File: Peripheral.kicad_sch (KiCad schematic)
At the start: 25 parts, among them J2 Conn_02x05_Odd_Even, J3 Conn_02x08_Odd_Even, J4 Conn_02x08_Odd_Even, J6 Bus_ISA_8bit, J7 Conn_02x17_Odd_Even, J8 TTL UART, U25 SN74LS07N, U3 74164, U31 TXS0104ED, U32 16550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

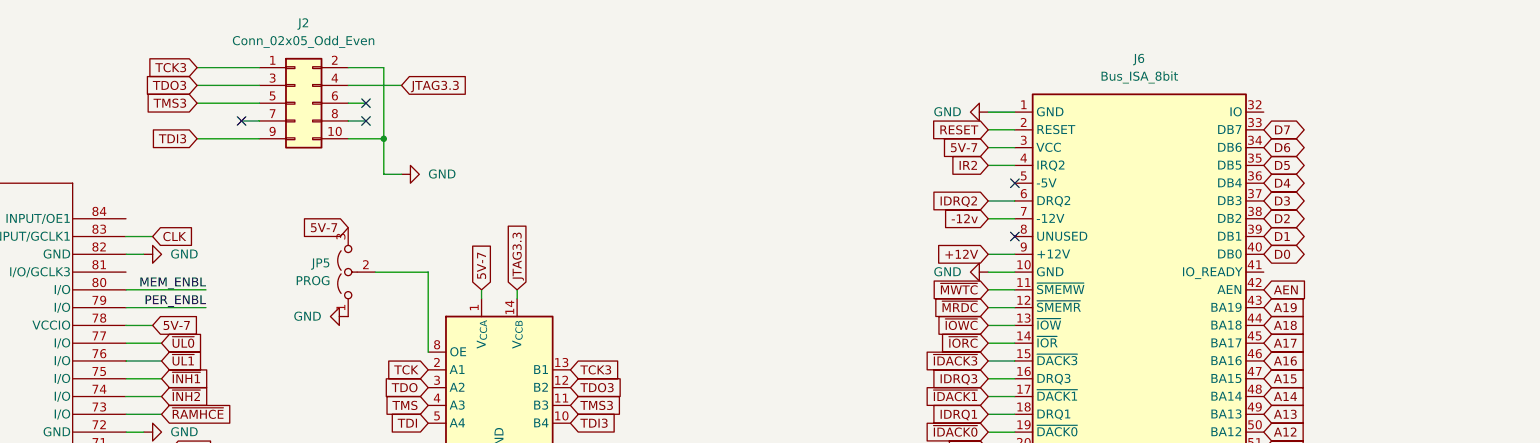
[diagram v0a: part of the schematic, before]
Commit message: Adjusted Data Bus for 80130
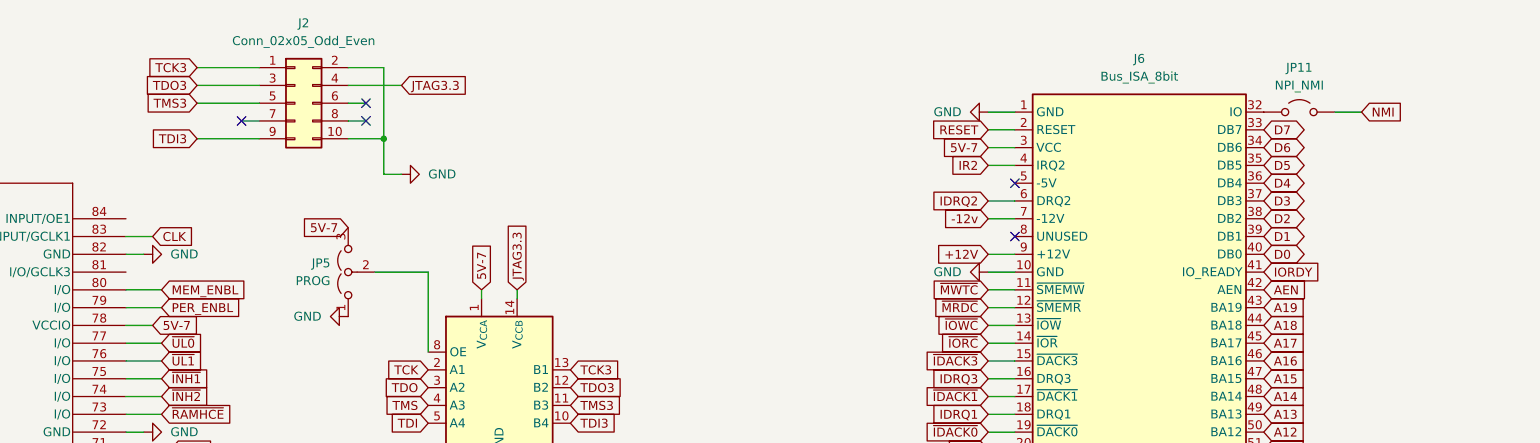
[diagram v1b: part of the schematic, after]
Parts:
- added JP11: NPI_NMI, symbol Jumper:Jumper_2_Open
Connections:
- net at J6.32 (IO): now also JP11.1 (A)
- net IORDY: now reaches J6.41 (IO_READY)
- new net NMI: JP11.2 (B)
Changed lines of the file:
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@@
 	(wire
 		(pts
-			(xy 163.83 55.88) (xy 152.4 55.88)
+			(xy 157.48 55.88) (xy 152.4 55.88)
 		)
 		(stroke
@@
 	(wire
 		(pts
-			(xy 163.83 58.42) (xy 152.4 58.42)
+			(xy 157.48 58.42) (xy 152.4 58.42)
 		)
 		(stroke
@@
 	(wire
 		(pts
+			(xy 328.93 30.48) (xy 325.12 30.48)
+		)
+		(stroke
+			(width 0)
+			(type default)
+		)
+	)
+	(wire
+		(pts
 			(xy 158.75 127) (xy 152.4 127)
 		)
@@
 	)
 	(label "MEM_ENBL"
-		(at 163.83 55.88 180)
-		(effects
-			(font
-				(size 1.27 1.27)
-			)
-			(justify right bottom)
-		)
-	)
-	(label "PER_ENBL"
-		(at 163.83 58.42 180)
-		(effects
-			(font
-				(size 1.27 1.27)
-			)
-			(justify right bottom)
-		)
-	)
-	(label "MEM_ENBL"
 		(at 40.64 261.62 0)
 		(effects
@@
 		)
 	)
+	(global_label "PER_ENBL"
+		(shape input)
+		(at 157.48 58.42 0)
+		(fields_autoplaced yes)
+		(effects
+			(font
+				(size 1.27 1.27)
+			)
+			(justify left)
+		)
+		(property "Intersheetrefs" "${INTERSHEET_REFS}"
+			(at 169.8994 58.42 0)
+			(effects
+				(font
+					(size 1.27 1.27)
+				)
+				(justify left)
+				(hide yes)
+			)
+		)
+	)
 	(global_label "~{MRDC}"
 		(shape input)
@@
 		)
 	)
+	(global_label "NMI"
+		(shape input)
+		(at 328.93 30.48 0)
+		(fields_autoplaced yes)
+		(effects
+			(font
+				(size 1.27 1.27)
+			)
+			(justify left)
+		)
+		(property "Intersheetrefs" "${INTERSHEET_REFS}"
+			(at 335.3019 30.48 0)
+			(effects
+				(font
+					(size 1.27 1.27)
+				)
+				(justify left)
+				(hide yes)
+			)
+		)
+	)
 	(global_label "~{IDACK0}"
 		(shape input)
@@
 		)
 	)
+	(global_label "IORDY"
+		(shape input)
+		(at 314.96 53.34 0)
+		(fields_autoplaced yes)
+		(effects
+			(font
+				(size 1.27 1.27)
+			)
+			(justify left)
+		)
+		(property "Intersheetrefs" "${INTERSHEET_REFS}"
+			(at 323.5091 53.34 0)
+			(effects
+				(font
+					(size 1.27 1.27)
+				)
+				(justify left)
+				(hide yes)
+			)
+		)
+	)
 	(global_label "A13"
 		(shape input)
@@
 		)
 	)
+	(global_label "MEM_ENBL"
+		(shape input)
+		(at 157.48 55.88 0)
+		(fields_autoplaced yes)
+		(effects
+			(font
+				(size 1.27 1.27)
+			)
+			(justify left)
+		)
+		(property "Intersheetrefs" "${INTERSHEET_REFS}"
+			(at 170.2622 55.88 0)
+			(effects
+				(font
+					(size 1.27 1.27)
+				)
+				(justify left)
+				(hide yes)
+			)
+		)
+	)
 	(global_label "5V-7"
 		(shape input)
@@
 					(unit 1)
 				)
+			)
+		)
+	)
+	(symbol
+		(lib_id "Jumper:Jumper_2_Open")
+		(at 320.04 30.48 0)
+		(unit 1)
+		(exclude_from_sim no)
+		(in_bom yes)
+		(on_board yes)
+		(dnp no)
+		(fields_autoplaced yes)
+		(property "Reference" "JP11"
+			(at 320.04 24.13 0)
+			(effects
+				(font
+					(size 1.27 1.27)
+				)
+			)
+		)
+		(property "Value" "NPI_NMI"
+			(at 320.04 26.67 0)
+			(effects
+				(font
+					(size 1.27 1.27)
+				)
+			)
+		)
+		(property "Footprint" ""
+			(at 320.04 30.48 0)
+			(effects
+				(font
+					(size 1.27 1.27)
+				)
+				(hide yes)
+			)
+		)
+		(property "Datasheet" "~"
+			(at 320.04 30.48 0)
+			(effects
+				(font
+					(size 1.27 1.27)
+				)
+				(hide yes)
+			)
+		)
+		(property "Description" "Jumper, 2-pole, open"
+			(at 320.04 30.48 0)
+			(effects
+				(font
+					(size 1.27 1.27)
+				)
+				(hide yes)
+			)
+		)
+		(pin "1"
+		)
+		(pin "2"
+		)
+		(instances
+			(project "8086MAX_SBC"
+				(path "/f3556896-fb91-4e69-9fe8-87bb2814f9d4/130d313c-ef1b-459f-b12a-6a2f6b18a216"
+					(reference "JP11")
+					(unit 1)
+				)

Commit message: assigned all footprints
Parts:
- C10, C11, C12, C13: footprint (none) -> Capacitor_THT:C_Disc_D8.0mm_W2.5mm_P5.00mm
- J2: footprint (none) -> Connector_PinHeader_2.54mm:PinHeader_2x05_P2.54mm_Vertical
- J3, J4: footprint (none) -> Connector_PinHeader_2.54mm:PinHeader_2x08_P2.54mm_Vertical
- J6: footprint (none) -> 7-5530843-0:TE_7-5530843-0
- J7: footprint (none) -> Connector_IDC:IDC-Header_2x17_P2.54mm_Latch_Vertical
- J8: footprint (none) -> Connector_PinHeader_2.54mm:PinHeader_1x05_P2.54mm_Vertical
- JP10, JP11, JP7, JP8, JP9: footprint (none) -> Connector_PinHeader_2.54mm:PinHeader_1x02_P2.54mm_Vertical
- JP5: footprint (none) -> Connector_PinHeader_2.54mm:PinHeader_1x03_P2.54mm_Vertical
- U25, U3, U6: footprint (none) -> Package_DIP:DIP-14_W7.62mm
- U33: footprint (none) -> Package_LCC:PLCC-44_THT-Socket
- U9: footprint PLCC84_MCH -> Package_LCC:PLCC-84_29.3x29.3mm_P1.27mm
- Y2, Y3: footprint (none) -> Crystal:Crystal_HC49-U_Vertical
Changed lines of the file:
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@@
 			)
 		)
-		(property "Footprint" ""
+		(property "Footprint" "Connector_PinHeader_2.54mm:PinHeader_2x05_P2.54mm_Vertical"
 			(at 176.53 29.21 0)
 			(effects
@@
 			)
 		)
-		(property "Footprint" ""
+		(property "Footprint" "Capacitor_THT:C_Disc_D8.0mm_W2.5mm_P5.00mm"
 			(at 300.6852 365.76 0)
 			(effects
@@
 			)
 		)
-		(property "Footprint" ""
+		(property "Footprint" "Connector_PinHeader_2.54mm:PinHeader_1x02_P2.54mm_Vertical"
 			(at 320.04 30.48 0)
 			(effects
@@
 			)
 		)
-		(property "Footprint" ""
+		(property "Footprint" "Package_DIP:DIP-14_W7.62mm"
 			(at 24.13 379.73 0)
 			(effects
@@
 			)
 		)
-		(property "Footprint" ""
+		(property "Footprint" "Connector_PinHeader_2.54mm:PinHeader_2x08_P2.54mm_Vertical"
 			(at 109.22 210.82 0)
 			(effects
@@
 			)
 		)
-		(property "Footprint" ""
+		(property "Footprint" "Package_DIP:DIP-14_W7.62mm"
 			(at 24.13 412.75 0)
 			(effects
@@
 			)
 		)
-		(property "Footprint" ""
+		(property "Footprint" "Connector_PinHeader_2.54mm:PinHeader_1x02_P2.54mm_Vertical"
 			(at 334.01 330.2 0)
 			(effects
@@
 			)
 		)
-		(property "Footprint" ""
+		(property "Footprint" "Package_DIP:DIP-14_W7.62mm"
 			(at 104.14 401.32 0)
 			(effects
@@
 			)
 		)
-		(property "Footprint" ""
+		(property "Footprint" "Connector_PinHeader_2.54mm:PinHeader_2x08_P2.54mm_Vertical"
 			(at 109.22 292.1 0)
 			(effects
@@
 			)
 		)
-		(property "Footprint" ""
+		(property "Footprint" "Package_DIP:DIP-14_W7.62mm"
 			(at 124.46 203.2 0)
 			(effects
@@
 			)
 		)
-		(property "Footprint" ""
+		(property "Footprint" "Crystal:Crystal_HC49-U_Vertical"
 			(at 320.04 358.14 0)
 			(effects
@@
 			)
 		)
-		(property "Footprint" ""
+		(property "Footprint" "Connector_PinHeader_2.54mm:PinHeader_1x02_P2.54mm_Vertical"
 			(at 274.32 372.11 0)
 			(effects
@@
 			)
 		)
-		(property "Footprint" ""
+		(property "Footprint" "Capacitor_THT:C_Disc_D8.0mm_W2.5mm_P5.00mm"
 			(at 324.8152 365.76 0)
 			(effects
@@
 			)
 		)
-		(property "Footprint" ""
+		(property "Footprint" "Connector_IDC:IDC-Header_2x17_P2.54mm_Latch_Vertical"
 			(at 375.92 304.8 0)
 			(effects
@@
 			)
 		)
-		(property "Footprint" ""
+		(property "Footprint" "Capacitor_THT:C_Disc_D8.0mm_W2.5mm_P5.00mm"
 			(at 291.1348 365.76 0)
 			(effects
@@
 			)
 		)
-		(property "Footprint" ""
+		(property "Footprint" "Crystal:Crystal_HC49-U_Vertical"
 			(at 295.91 358.14 0)
 			(effects
@@
 			)
 		)
-		(property "Footprint" ""
+		(property "Footprint" "Package_DIP:DIP-14_W7.62mm"
 			(at 24.13 396.24 0)
 			(effects
@@
 			)
 		)
-		(property "Footprint" ""
+		(property "Footprint" "7-5530843-0:TE_7-5530843-0"
 			(at 297.18 68.58 0)
 			(effects
@@
 			)
 		)
-		(property "Footprint" ""
+		(property "Footprint" "Package_DIP:DIP-14_W7.62mm"
 			(at 24.13 364.49 0)
 			(effects
@@
 			)
 		)
-		(property "Footprint" ""
+		(property "Footprint" "Package_DIP:DIP-14_W7.62mm"
 			(at 71.12 193.04 0)
 			(effects
@@
 			)
 		)
-		(property "Footprint" ""
+		(property "Footprint" "Package_DIP:DIP-14_W7.62mm"
 			(at 71.12 274.32 0)
 			(effects
@@
 			)
 		)
-		(property "Footprint" ""
+		(property "Footprint" "Capacitor_THT:C_Disc_D8.0mm_W2.5mm_P5.00mm"
 			(at 315.2648 365.76 0)
 			(effects
@@
 			)
 		)
-		(property "Footprint" ""
+		(property "Footprint" "Package_LCC:PLCC-44_THT-Socket"
 			(at 266.7 323.85 0)
 			(effects
@@
 					(size 1.27 1.27)
 				)
+				(hide yes)
 			)
 		)
@@
 			)
 		)
-		(property "Footprint" ""
+		(property "Footprint" "Connector_PinHeader_2.54mm:PinHeader_1x02_P2.54mm_Vertical"
 			(at 227.33 334.01 0)
 			(effects
@@
 			)
 		)
-		(property "Footprint" ""
+		(property "Footprint" "Package_DIP:DIP-14_W7.62mm"
 			(at 124.46 284.48 0)
 			(effects
@@
 			)
 		)
-		(property "Footprint" ""
+		(property "Footprint" "Connector_PinHeader_2.54mm:PinHeader_1x02_P2.54mm_Vertical"
 			(at 276.86 359.41 0)
 			(effects
@@
 			)
 		)
-		(property "Footprint" ""
+		(property "Footprint" "Connector_PinHeader_2.54mm:PinHeader_1x05_P2.54mm_Vertical"
 			(at 289.56 168.91 0)
 			(effects
@@
 			)
 		)
-		(property "Footprint" ""
+		(property "Footprint" "Connector_PinHeader_2.54mm:PinHeader_1x03_P2.54mm_Vertical"
 			(at 184.15 53.34 0)
 			(effects
@@
 			)
 		)
-		(property "Footprint" "PLCC84_MCH"
+		(property "Footprint" "Package_LCC:PLCC-84_29.3x29.3mm_P1.27mm"
 			(at 50.8 45.72 0)
 			(effects

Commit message: Updated PCB
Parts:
- added C32, C33, C34, C35, C36, C37: 0.1uF, Capacitor_THT:C_Disc_D8.0mm_W2.5mm_P5.00mm, symbol Device:C
- U9: footprint Package_LCC:PLCC-84_29.3x29.3mm_P1.27mm -> Package_LCC:PLCC-84_THT-Socket
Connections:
- net GND: now also C32.2, C33.2, C34.2, C35.2, C36.2, C37.2
- net VCC: now also C32.1, C33.1, C34.1, C35.1, C36.1, C37.1
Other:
- moved on the sheet: U25G

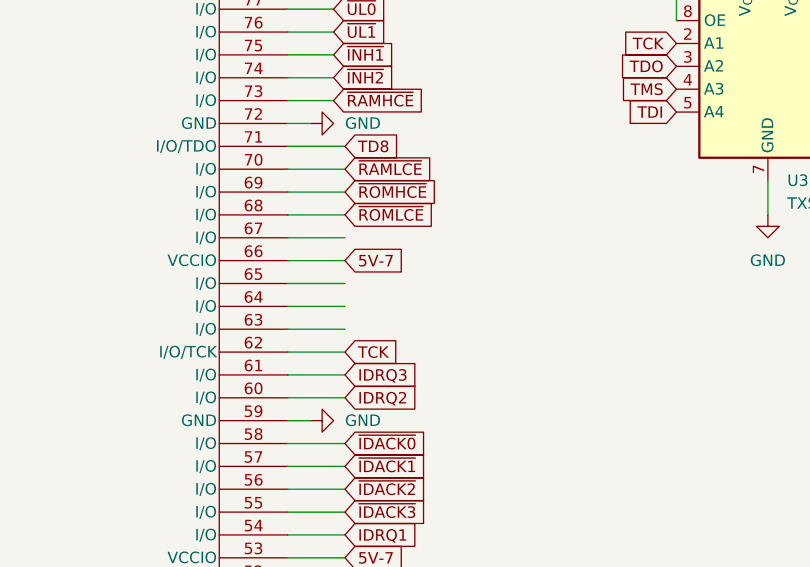
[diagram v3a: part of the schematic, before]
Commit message: Fixed missing nets
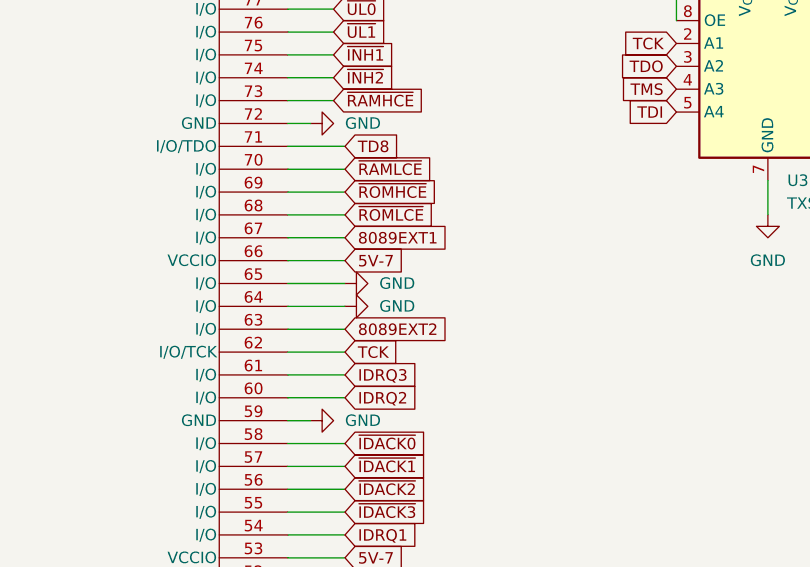
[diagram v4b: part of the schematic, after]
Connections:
- net GND: now also U9.64 (I/O), U9.65 (I/O)
- net 8089EXT2: now reaches U9.63 (I/O)
- net 8089EXT1: now reaches U9.67 (I/O)
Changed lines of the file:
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@@
 		)
 	)
+	(global_label "8089EXT2"
+		(shape input)
+		(at 158.75 99.06 0)
+		(fields_autoplaced yes)
+		(effects
+			(font
+				(size 1.27 1.27)
+			)
+			(justify left)
+		)
+		(property "Intersheetrefs" "${INTERSHEET_REFS}"
+			(at 171.1088 99.06 0)
+			(effects
+				(font
+					(size 1.27 1.27)
+				)
+				(justify left)
+				(hide yes)
+			)
+		)
+	)
 	(global_label "5V-7"
 		(shape input)
@@
 		)
 	)
+	(global_label "8089EXT1"
+		(shape input)
+		(at 158.75 88.9 0)
+		(fields_autoplaced yes)
+		(effects
+			(font
+				(size 1.27 1.27)
+			)
+			(justify left)
+		)
+		(property "Intersheetrefs" "${INTERSHEET_REFS}"
+			(at 171.1088 88.9 0)
+			(effects
+				(font
+					(size 1.27 1.27)
+				)
+				(justify left)
+				(hide yes)
+			)
+		)
+	)
 	(global_label "5V-7"
 		(shape input)
@@
 		)
 		(instances
-			(project ""
+			(project "8086MAX_SBC"
 				(path "/f3556896-fb91-4e69-9fe8-87bb2814f9d4/130d313c-ef1b-459f-b12a-6a2f6b18a216"
 					(reference "U32")
@@
 		)
 		(instances
-			(project ""
+			(project "8086MAX_SBC"
 				(path "/f3556896-fb91-4e69-9fe8-87bb2814f9d4/130d313c-ef1b-459f-b12a-6a2f6b18a216"
 					(reference "RN5")
@@
 		)
 		(instances
-			(project ""
+			(project "8086MAX_SBC"
 				(path "/f3556896-fb91-4e69-9fe8-87bb2814f9d4/130d313c-ef1b-459f-b12a-6a2f6b18a216"
 					(reference "U25")
@@
 		)
 		(instances
-			(project ""
+			(project "8086MAX_SBC"
 				(path "/f3556896-fb91-4e69-9fe8-87bb2814f9d4/130d313c-ef1b-459f-b12a-6a2f6b18a216"
 					(reference "J3")
@@
 		)
 		(instances
-			(project ""
+			(project "8086MAX_SBC"
 				(path "/f3556896-fb91-4e69-9fe8-87bb2814f9d4/130d313c-ef1b-459f-b12a-6a2f6b18a216"
 					(reference "U25")
@@
 		)
 		(instances
-			(project ""
+			(project "8086MAX_SBC"
 				(path "/f3556896-fb91-4e69-9fe8-87bb2814f9d4/130d313c-ef1b-459f-b12a-6a2f6b18a216"
 					(reference "U25")
@@
 		)
 		(instances
-			(project ""
+			(project "8086MAX_SBC"
 				(path "/f3556896-fb91-4e69-9fe8-87bb2814f9d4/130d313c-ef1b-459f-b12a-6a2f6b18a216"
 					(reference "U31")
@@
 		)
 		(instances
-			(project ""
+			(project "8086MAX_SBC"
 				(path "/f3556896-fb91-4e69-9fe8-87bb2814f9d4/130d313c-ef1b-459f-b12a-6a2f6b18a216"
 					(reference "U25")
@@
 		)
 		(instances
-			(project ""
+			(project "8086MAX_SBC"
 				(path "/f3556896-fb91-4e69-9fe8-87bb2814f9d4/130d313c-ef1b-459f-b12a-6a2f6b18a216"
 					(reference "J7")
@@
 		)
 		(instances
-			(project ""
+			(project "8086MAX_SBC"
 				(path "/f3556896-fb91-4e69-9fe8-87bb2814f9d4/130d313c-ef1b-459f-b12a-6a2f6b18a216"
 					(reference "Y2")
@@
 		)
 		(instances
-			(project ""
+			(project "8086MAX_SBC"
 				(path "/f3556896-fb91-4e69-9fe8-87bb2814f9d4/130d313c-ef1b-459f-b12a-6a2f6b18a216"
 					(reference "U25")
@@
 		)
 		(instances
-			(project ""
+			(project "8086MAX_SBC"
 				(path "/f3556896-fb91-4e69-9fe8-87bb2814f9d4/130d313c-ef1b-459f-b12a-6a2f6b18a216"
 					(reference "J6")
@@
 		)
 		(instances
-			(project ""
+			(project "8086MAX_SBC"
 				(path "/f3556896-fb91-4e69-9fe8-87bb2814f9d4/130d313c-ef1b-459f-b12a-6a2f6b18a216"
 					(reference "U25")
@@
 		)
 		(instances
-			(project ""
+			(project "8086MAX_SBC"
 				(path "/f3556896-fb91-4e69-9fe8-87bb2814f9d4/130d313c-ef1b-459f-b12a-6a2f6b18a216"
 					(reference "U3")
@@
 	)
 	(symbol
+		(lib_id "power:GND")
+		(at 158.75 96.52 90)
+		(unit 1)
+		(exclude_from_sim no)
+		(in_bom yes)
+		(on_board yes)
+		(dnp no)
+		(fields_autoplaced yes)
+		(property "Reference" "#PWR063"
+			(at 165.1 96.52 0)
+			(effects
+				(font
+					(size 1.27 1.27)
+				)
+				(hide yes)
+			)
+		)
+		(property "Value" "GND"
+			(at 162.56 96.5199 90)
+			(effects
+				(font
+					(size 1.27 1.27)
+				)
+				(justify right)
+			)
+		)
+		(property "Footprint" ""
+			(at 158.75 96.52 0)
+			(effects
+				(font
+					(size 1.27 1.27)
+				)
+				(hide yes)
+			)
+		)
+		(property "Datasheet" ""
+			(at 158.75 96.52 0)
+			(effects
+				(font
+					(size 1.27 1.27)
+				)
+				(hide yes)
+			)
+		)
+		(property "Description" "Power symbol creates a global label with name \"GND\" , ground"
+			(at 158.75 96.52 0)
+			(effects
+				(font
+					(size 1.27 1.27)
+				)
+				(hide yes)
+			)
+		)
+		(pin "1"
+		)
+		(instances
+			(project "8086MAX_SBC"
+				(path "/f3556896-fb91-4e69-9fe8-87bb2814f9d4/130d313c-ef1b-459f-b12a-6a2f6b18a216"
+					(reference "#PWR063")
+					(unit 1)
+				)
+			)
+		)
+	)
+	(symbol
 		(lib_id "Device:C")
 		(at 78.74 398.78 0)
@@
 		)
 		(instances
-			(project ""
+			(project "8086MAX_SBC"
 				(path "/f3556896-fb91-4e69-9fe8-87bb2814f9d4/130d313c-ef1b-459f-b12a-6a2f6b18a216"
 					(reference "U33")
@@
 		)
 		(instances
-			(project ""
+			(project "8086MAX_SBC"
 				(path "/f3556896-fb91-4e69-9fe8-87bb2814f9d4/130d313c-ef1b-459f-b12a-6a2f6b18a216"
 					(reference "U25")
@@
 	)
 	(symbol
+		(lib_id "power:GND")
+		(at 158.75 93.98 90)
+		(unit 1)
+		(exclude_from_sim no)
+		(in_bom yes)
+		(on_board yes)
+		(dnp no)
+		(fields_autoplaced yes)
+		(property "Reference" "#PWR062"
+			(at 165.1 93.98 0)
+			(effects
+				(font
+					(size 1.27 1.27)
+				)
+				(hide yes)
+			)
+		)
+		(property "Value" "GND"
+			(at 162.56 93.9799 90)
+			(effects
+				(font
+					(size 1.27 1.27)
+				)
+				(justify right)
+			)
+		)
+		(property "Footprint" ""
+			(at 158.75 93.98 0)
+			(effects
+				(font
+					(size 1.27 1.27)
+				)
+				(hide yes)
+			)
+		)
+		(property "Datasheet" ""
+			(at 158.75 93.98 0)
+			(effects
+				(font
+					(size 1.27 1.27)
+				)
+				(hide yes)
+			)
+		)
+		(property "Description" "Power symbol creates a global label with name \"GND\" , ground"
+			(at 158.75 93.98 0)
+			(effects
+				(font
+					(size 1.27 1.27)
+				)
+				(hide yes)
+			)
+		)
+		(pin "1"
+		)
+		(instances
+			(project "8086MAX_SBC"
+				(path "/f3556896-fb91-4e69-9fe8-87bb2814f9d4/130d313c-ef1b-459f-b12a-6a2f6b18a216"
+					(reference "#PWR062")
+					(unit 1)
+				)
+			)
+		)
+	)
+	(symbol
 		(lib_id "Jumper:Jumper_2_Open")
 		(at 276.86 359.41 90)
@@
 		)
 		(instances
-			(project ""
+			(project "8086MAX_SBC"
 				(path "/f3556896-fb91-4e69-9fe8-87bb2814f9d4/130d313c-ef1b-459f-b12a-6a2f6b18a216"
 					(reference "JP7")
@@
 		)
 		(instances
-			(project ""
+			(project "8086MAX_SBC"
 				(path "/f3556896-fb91-4e69-9fe8-87bb2814f9d4/130d313c-ef1b-459f-b12a-6a2f6b18a216"
 					(reference "J8")
@@
 		)
 		(instances
-			(project ""
+			(project "8086MAX_SBC"
 				(path "/f3556896-fb91-4e69-9fe8-87bb2814f9d4/130d313c-ef1b-459f-b12a-6a2f6b18a216"
 					(reference "JP5")
